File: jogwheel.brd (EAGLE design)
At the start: 100 x 52 mm, 61 parts, among them IC1 FT232RL

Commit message: Parts in are in correct places (4 line opto version).
Few traces done. Not many however.
Fixed silkscreen slightly.
First version ordered from iteadstudios.
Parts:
- removed 2.U0, 2.U1, 5.U0: OPTO_2_CHANNELSACPL-827-300E, jogwheel_parts:ACPL-825
- removed 8.T0, 8.T1, 8.T2, 8.T3, 8.T4, 8.T5, 8.T6, 8.T7: CONNECTOR_2PIN2W-TERMINAL-HEADER-20.155MV/2, connectors:2WAY-TERMINAL-HEADER-20.155MV/2
- removed C1, C3, C5: 100nF, RC_and_L:C0805
- added 0.C3, 0.C4, 1.C4: 100nF, RC_and_L:C0805
- added 5.R10, 5.R11, 5.R12, 5.R13, 5.R14, 5.R15, 5.R16, 5.R17, 5.R18, 5.R19, 5.R20, 5.R21, 5.R22, 5.R23, 5.R4, 5.R5, 5.R6, 5.R7, 5.R8, 5.R9: 10k, RC_and_L:R0805
- added 5.T10, 5.T11, 5.T2, 5.T3, 5.T4, 5.T5, 5.T6, 5.T7, 5.T8, 5.T9: CONNECTOR_2PIN2W-TERMINAL-HEADER-20.155MV/2, connectors:2WAY-TERMINAL-HEADER-20.155MV/2
- added IC2, IC3, IC4, IC5: OPTO_4_CHANNELS, jogwheel_parts:ACPL-845-O300
- moved 5.R3 274.0 mm to (15.2, 31.8), turned to 90 degrees
- moved 0.C2 258.3 mm to (70.4, 51.1), turned to 90 degrees
- moved 5.R1 256.9 mm to (10.2, 31.8), turned to 90 degrees
- moved 5.R2 252.8 mm to (12.7, 13.3), turned to 270 degrees
- moved 5.R0 234.6 mm to (7.62, 13.3), turned to 270 degrees
- moved 1.C2 233.7 mm to (48.5, 37.6)
- moved 1.L1 233.3 mm to (48.5, 39.8), turned to 180 degrees
- moved 1.C1 224.3 mm to (30.5, 40.8), turned to 180 degrees
- moved 1.C0 223.9 mm to (30.5, 43.0), turned to 180 degrees
- moved 2.R6 193.8 mm to (22.9, 33.7), turned to 270 degrees
- moved 2.R4 187.0 mm to (17.8, 33.7), turned to 270 degrees
- moved 2.R2 180.4 mm to (12.7, 33.7), turned to 270 degrees
- moved 2.R3 175.9 mm to (16.5, 50.8), turned to 180 degrees
- moved 2.R0 173.7 mm to (7.62, 33.7), turned to 270 degrees
- moved 2.R1 172.2 mm to (10.2, 50.8), turned to 180 degrees
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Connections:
- net N$13 renamed AVCC
- removed net VCC: 0.C0.+, 0.C1.1
- new net N$12: 5.R4.1, IC3.5
- new net N$14: 5.R5.1, IC3.7
- new net N$25: 5.T3.2, IC3.8
- new net N$26: 5.R5.2, 5.T3.1
- new net N$27: 5.T2.2, IC3.6
- new net N$28: 5.R4.2, 5.T2.1
- new net N$29: 5.R8.1, IC4.1
- new net N$30: 5.R10.1, IC4.3
- new net N$31: 5.T5.2, IC4.4
- new net N$32: 5.R10.2, 5.T5.1
- new net N$33: 5.T4.2, IC4.2
- new net N$34: 5.R8.2, 5.T4.1
- new net N$35: 5.R12.1, IC4.5
- new net N$36: 5.R13.1, IC4.7
- new net N$37: 5.T7.2, IC4.8
- new net N$38: 5.R13.2, 5.T7.1
- new net N$39: 5.T6.2, IC4.6
- new net N$40: 5.R12.2, 5.T6.1
- new net N$41: 5.R16.1, IC5.1
- new net N$42: 5.R18.1, IC5.3
- new net N$43: 5.T9.2, IC5.4
- new net N$44: 5.R18.2, 5.T9.1
- new net N$45: 5.T8.2, IC5.2
- new net N$46: 5.R16.2, 5.T8.1
- new net N$47: 5.R20.1, IC5.5
- new net N$48: 5.R21.1, IC5.7
- new net N$49: 5.T11.2, IC5.8
- new net N$50: 5.R21.2, 5.T11.1
- new net N$51: 5.T10.2, IC5.6
- new net N$52: 5.R20.2, 5.T10.1
- net +24V: now also 4.T4.2, IC2.10, IC2.12, IC2.14, IC2.16; no longer 2.U0.6, 2.U0.8, 2.U1.6, 2.U1.8, 4.T4.1
- net +3V3: now also 1.C4.1; no longer 0.C2.1
- net +5V: now also 0.C0.+, 0.C1.1, 0.C2.1, 0.C3.1, IC3.10, IC3.12, IC3.14, IC3.16, IC4.10, IC4.12, IC4.14, IC4.16, IC5.10, IC5.12, IC5.14, IC5.16; no longer 5.U0.6, 5.U0.8, C3.1, C5.1
- net AGND: now also 4.T4.1; no longer 4.T4.2
- net B2: now also 5.R14.1, IC4.11
- net C0: now also 5.R15.1, IC4.9; no longer 8.T0.2
- net C1: now also 5.R17.1, IC5.15; no longer 8.T1.2
- net C2: now also 5.R19.1, IC5.13; no longer 8.T2.2
- net C3: now also 5.R22.1, IC5.11; no longer 8.T3.2
- net C4: now also 5.R23.1, IC5.9; no longer 8.T4.2
- net C5: no longer 8.T5.2
- net D2: now also IC3.15; no longer 5.U0.5
- net D3: now also IC3.13; no longer 5.U0.7
- net D4: now also 5.R6.1, IC3.11
- net D5: now also 5.R7.1, IC3.9
- net D6: now also 5.R9.1, IC4.15; no longer 8.T6.2
- net D7: now also 5.R11.1, IC4.13; no longer 8.T7.2
- net GND: now also 0.C3.2, 0.C4.2, 1.C4.2, 5.R11.2, 5.R14.2, 5.R15.2, 5.R17.2, 5.R19.2, 5.R22.2, 5.R23.2, 5.R6.2, 5.R7.2, 5.R9.2, IC2.2, IC2.4, IC2.6, IC2.8; no longer 2.U0.2, 2.U0.4, 2.U1.2, 2.U1.4, 8.T0.1, 8.T1.1, 8.T2.1, 8.T3.1, 8.T4.1, 8.T5.1, 8.T6.1, 8.T7.1, C1.2, C3.2, C5.2
- net N$11: now also IC2.15; no longer 2.U0.5
- net N$15: now also IC3.3; no longer 5.U0.1
- net N$16: now also IC2.1; no longer 2.U0.3
- net N$17: now also IC2.7; no longer 2.U1.1
- net N$19: now also IC2.5; no longer 2.U1.3
- net N$20: now also IC3.1; no longer 5.U0.3
- net N$21: now also IC2.3; no longer 2.U0.1
- net N$22: now also IC3.2; no longer 5.U0.4
- net N$23: now also IC3.4; no longer 5.U0.2
- net N$5: now also IC2.11; no longer 2.U1.5
- net N$6: now also IC2.9; no longer 2.U1.7
- net N$7: now also 0.C4.1; no longer C1.1
- net N$9: now also IC2.13; no longer 2.U0.7
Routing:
- net C4: track 0.00 -> 57.8 mm, vias 0 -> 2
- net +5V: track 0.00 -> 56.8 mm
- net C3: track 0.00 -> 51.7 mm, vias 0 -> 2
- net ADC7: track 0.00 -> 50.0 mm, vias 0 -> 1
- net ADC6: track 0.00 -> 48.5 mm, vias 0 -> 1
- net C2: track 0.00 -> 43.3 mm, vias 0 -> 2
- net C1: track 0.00 -> 42.1 mm, vias 0 -> 2
- net D2: track 0.00 -> 41.5 mm, vias 0 -> 2
- net TXD: track 0.00 -> 38.2 mm, vias 0 -> 2
- net B0: track 0.00 -> 36.3 mm, vias 0 -> 2
- net RXD: track 0.00 -> 35.8 mm, vias 0 -> 2
- net B1: track 0.00 -> 34.8 mm, vias 0 -> 2
- net D3: track 0.00 -> 33.8 mm, vias 0 -> 2
- net D4: track 0.00 -> 28.9 mm, vias 0 -> 2
- net C0: track 0.00 -> 28.7 mm, vias 0 -> 2
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- added copper zone on layer 1, net +24V
- added copper zone on layer 16, net +24V
- added copper zone on layer 1, net +3V3
- added copper zone on layer 1, net +5V
- added copper zone on layer 1, net AGND
- added copper zone on layer 16, net AGND
- added copper zone on layer 1, net GND
- added copper zone on layer 16, net GND
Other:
- board size 100 x 52 mm -> 100 x 77 mm
- board text added: ""Relays""
- board text added: "ADC"
- board text added: "Inputs"
- board text added: "Power input"
- board text added: "Savpek Electronics"
- board text added: "USB-IO CARD"
- board text added: "v.25.01.2012"

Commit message: Fixed usart txd/rxd error from board.
Accidently, RXD/TXD wasn't crossed...
Now fixed!
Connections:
- net RXD: now also 1.MCU1.30; no longer 1.MCU1.31
- net TXD: now also 1.MCU1.31; no longer 1.MCU1.30
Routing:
- net RXD: track 35.8 -> 33.0 mm
- net TXD: track 38.2 -> 36.0 mm
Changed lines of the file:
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@@
 <setting verticaltext="up"/>
 </settings>
-<grid distance="0.2" unitdist="mm" unit="mm" style="lines" multiple="1" display="yes" altdistance="0.635" altunitdist="mm" altunit="mm"/>
+<grid distance="1.27" unitdist="mm" unit="mm" style="lines" multiple="1" display="yes" altdistance="0.635" altunitdist="mm" altunit="mm"/>
 <layers>
 <layer number="1" name="Top" color="4" fill="1" visible="yes" active="yes"/>
@@
 <layer number="25" name="tNames" color="7" fill="1" visible="yes" active="yes"/>
 <layer number="26" name="bNames" color="7" fill="1" visible="yes" active="yes"/>
-<layer number="27" name="tValues" color="7" fill="1" visible="no" active="yes"/>
+<layer number="27" name="tValues" color="7" fill="1" visible="yes" active="yes"/>
 <layer number="28" name="bValues" color="7" fill="1" visible="no" active="yes"/>
 <layer number="29" name="tStop" color="7" fill="3" visible="yes" active="yes"/>
@@
 <signals>
 <signal name="TXD">
-<contactref element="1.MCU1" pad="30"/>
 <contactref element="IC1" pad="5"/>
 <wire x1="65.16" y1="38.92" x2="65.16" y2="40.631" width="0.3048" layer="1"/>
@@
 <wire x1="44.323" y1="51.308" x2="42.672" y2="49.657" width="0.3048" layer="16"/>
 <wire x1="42.672" y1="49.657" x2="39.37" y2="49.657" width="0.3048" layer="16"/>
-<wire x1="38.17" y1="46.0751" x2="38.17" y2="48.33" width="0.3048" layer="1"/>
 <wire x1="38.17" y1="48.33" x2="38.354" y2="48.514" width="0.3048" layer="1"/>
 <wire x1="38.354" y1="48.514" x2="38.354" y2="49.149" width="0.3048" layer="1"/>
@@
 <via x="39.116" y="49.911" extent="1-16" drill="0.6096"/>
 <wire x1="39.116" y1="49.911" x2="39.37" y2="49.657" width="0.3048" layer="16"/>
+<contactref element="1.MCU1" pad="31"/>
+<wire x1="37.37" y1="46.0751" x2="38.17" y2="48.33" width="0" layer="19" extent="1-1"/>
 </signal>
 <signal name="RXD">
-<contactref element="1.MCU1" pad="31"/>
 <contactref element="IC1" pad="1"/>
-<wire x1="37.37" y1="46.0751" x2="37.37" y2="48.863" width="0.3048" layer="1"/>
 <wire x1="37.37" y1="48.863" x2="37.338" y2="48.895" width="0.3048" layer="1"/>
 <via x="37.338" y="48.895" extent="1-16" drill="0.6096"/>
@@
 <wire x1="62.56" y1="38.92" x2="62.56" y2="41.478" width="0.3048" layer="1"/>
 <wire x1="62.56" y1="41.478" x2="62.611" y2="41.529" width="0.3048" layer="1"/>
+<contactref element="1.MCU1" pad="30"/>
+<wire x1="38.17" y1="46.0751" x2="37.37" y2="48.863" width="0" layer="19" extent="1-1"/>
 </signal>
 <signal name="D2">

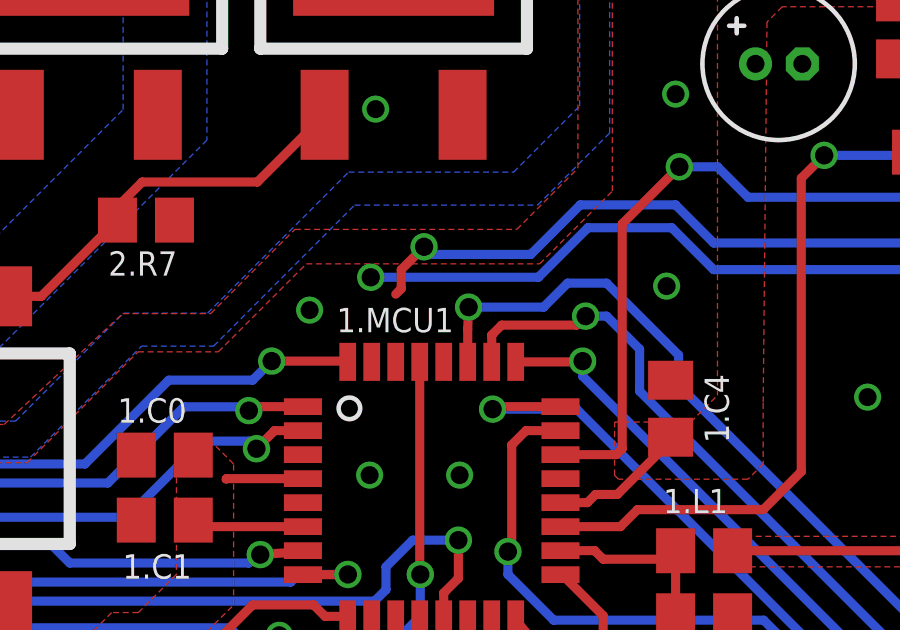
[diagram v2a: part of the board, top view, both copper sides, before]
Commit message: Fixed RX/TX in board layout.
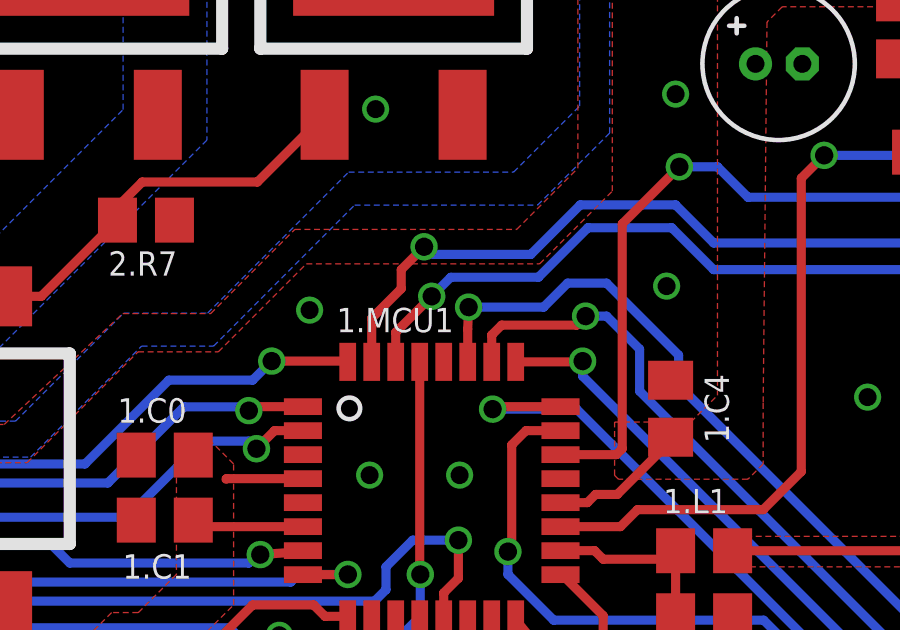
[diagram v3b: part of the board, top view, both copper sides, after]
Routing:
- net TXD: track 36.0 -> 38.6 mm
- net RXD: track 33.0 -> 33.8 mm
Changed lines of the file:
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@@
 <wire x1="44.323" y1="51.308" x2="42.672" y2="49.657" width="0.3048" layer="16"/>
 <wire x1="42.672" y1="49.657" x2="39.37" y2="49.657" width="0.3048" layer="16"/>
-<wire x1="38.17" y1="48.33" x2="38.354" y2="48.514" width="0.3048" layer="1"/>
 <wire x1="38.354" y1="48.514" x2="38.354" y2="49.149" width="0.3048" layer="1"/>
 <wire x1="38.354" y1="49.149" x2="39.116" y2="49.911" width="0.3048" layer="1"/>
@@
 <wire x1="39.116" y1="49.911" x2="39.37" y2="49.657" width="0.3048" layer="16"/>
 <contactref element="1.MCU1" pad="31"/>
-<wire x1="37.37" y1="46.0751" x2="38.17" y2="48.33" width="0" layer="19" extent="1-1"/>
+<wire x1="38.354" y1="48.514" x2="37.37" y2="47.53" width="0.3048" layer="1"/>
+<wire x1="37.37" y1="46.0751" x2="37.37" y2="47.53" width="0.3048" layer="1"/>
 </signal>
 <signal name="RXD">
 <contactref element="IC1" pad="1"/>
-<wire x1="37.37" y1="48.863" x2="37.338" y2="48.895" width="0.3048" layer="1"/>
-<via x="37.338" y="48.895" extent="1-16" drill="0.6096"/>
-<wire x1="37.338" y1="48.895" x2="42.926" y2="48.895" width="0.3048" layer="16"/>
 <wire x1="42.926" y1="48.895" x2="44.577" y2="50.546" width="0.3048" layer="16"/>
 <wire x1="44.577" y1="50.546" x2="47.371" y2="50.546" width="0.3048" layer="16"/>
@@
 <wire x1="62.56" y1="41.478" x2="62.611" y2="41.529" width="0.3048" layer="1"/>
 <contactref element="1.MCU1" pad="30"/>
-<wire x1="38.17" y1="46.0751" x2="37.37" y2="48.863" width="0" layer="19" extent="1-1"/>
+<wire x1="42.926" y1="48.895" x2="40.005" y2="48.895" width="0.3048" layer="16"/>
+<wire x1="40.005" y1="48.895" x2="39.37" y2="48.26" width="0.3048" layer="16"/>
+<via x="39.37" y="48.26" extent="1-16" drill="0.6096"/>
+<wire x1="39.37" y1="48.26" x2="38.17" y2="47.06" width="0.3048" layer="1"/>
+<wire x1="38.17" y1="46.0751" x2="38.17" y2="47.06" width="0.3048" layer="1"/>
 </signal>
 <signal name="D2">
